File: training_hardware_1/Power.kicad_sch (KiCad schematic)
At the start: 3 parts, among them U2 OKI

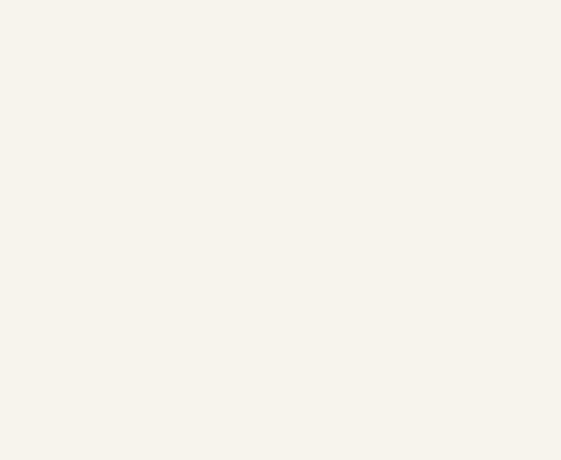
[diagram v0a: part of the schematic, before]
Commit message: Add Ethernet
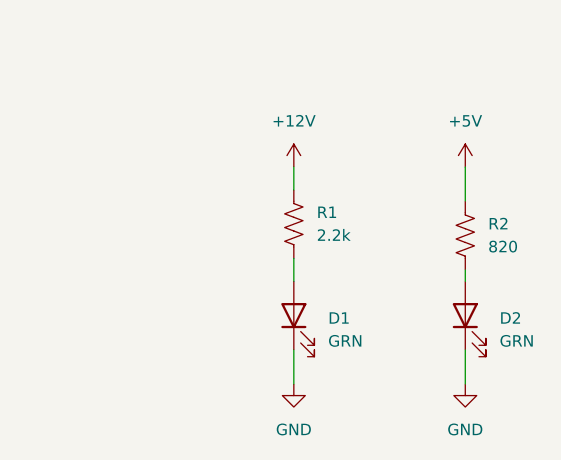
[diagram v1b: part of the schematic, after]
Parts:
- added D1, D2: GRN, symbol Device:LED
- added R1: 2.2k, symbol Device:R_US
- added R2: 820, symbol Device:R_US
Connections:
- net +12V: now also R1.1
- net +5V: now also R2.1
- net GND: now also D1.1 (K), D2.1 (K)
- new net: D1.2 (A), R1.2
- new net: D2.2 (A), R2.2
